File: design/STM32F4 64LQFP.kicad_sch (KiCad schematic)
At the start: 17 parts, among them P2 SWD, U1 STM32F40X_LQFP64, X2 8MHz 10ppm

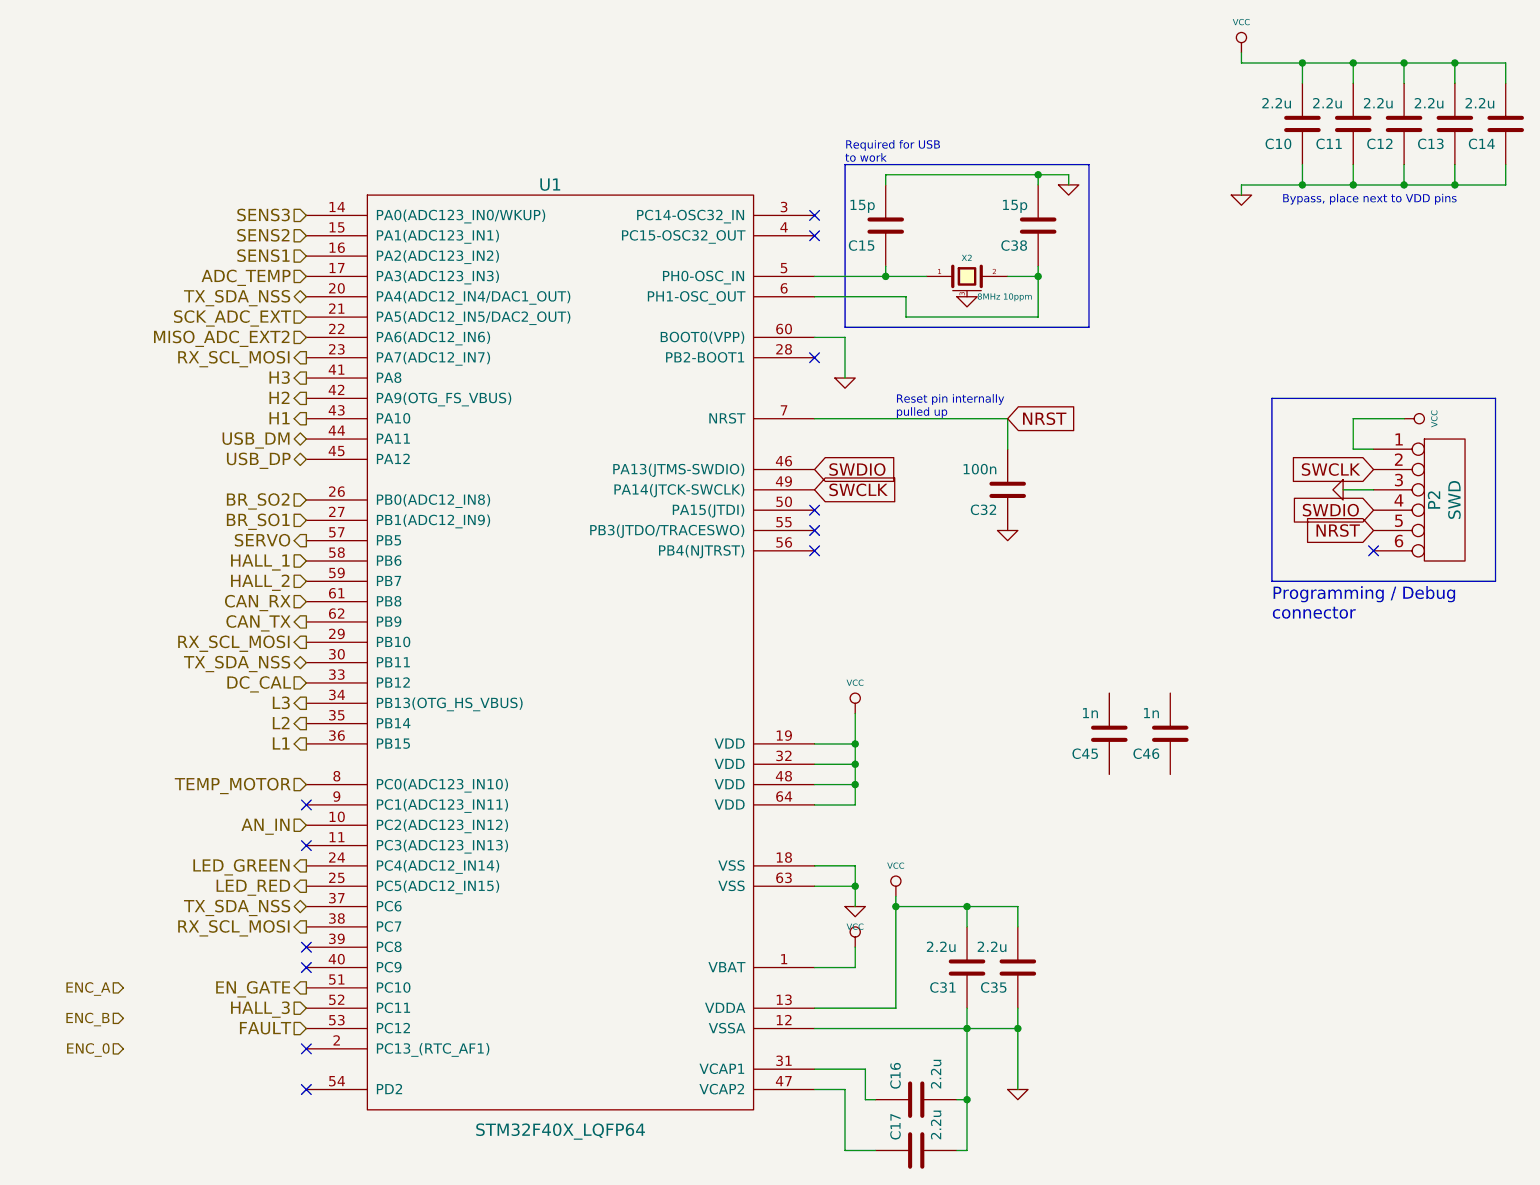
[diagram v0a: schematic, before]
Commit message: STM pins connected
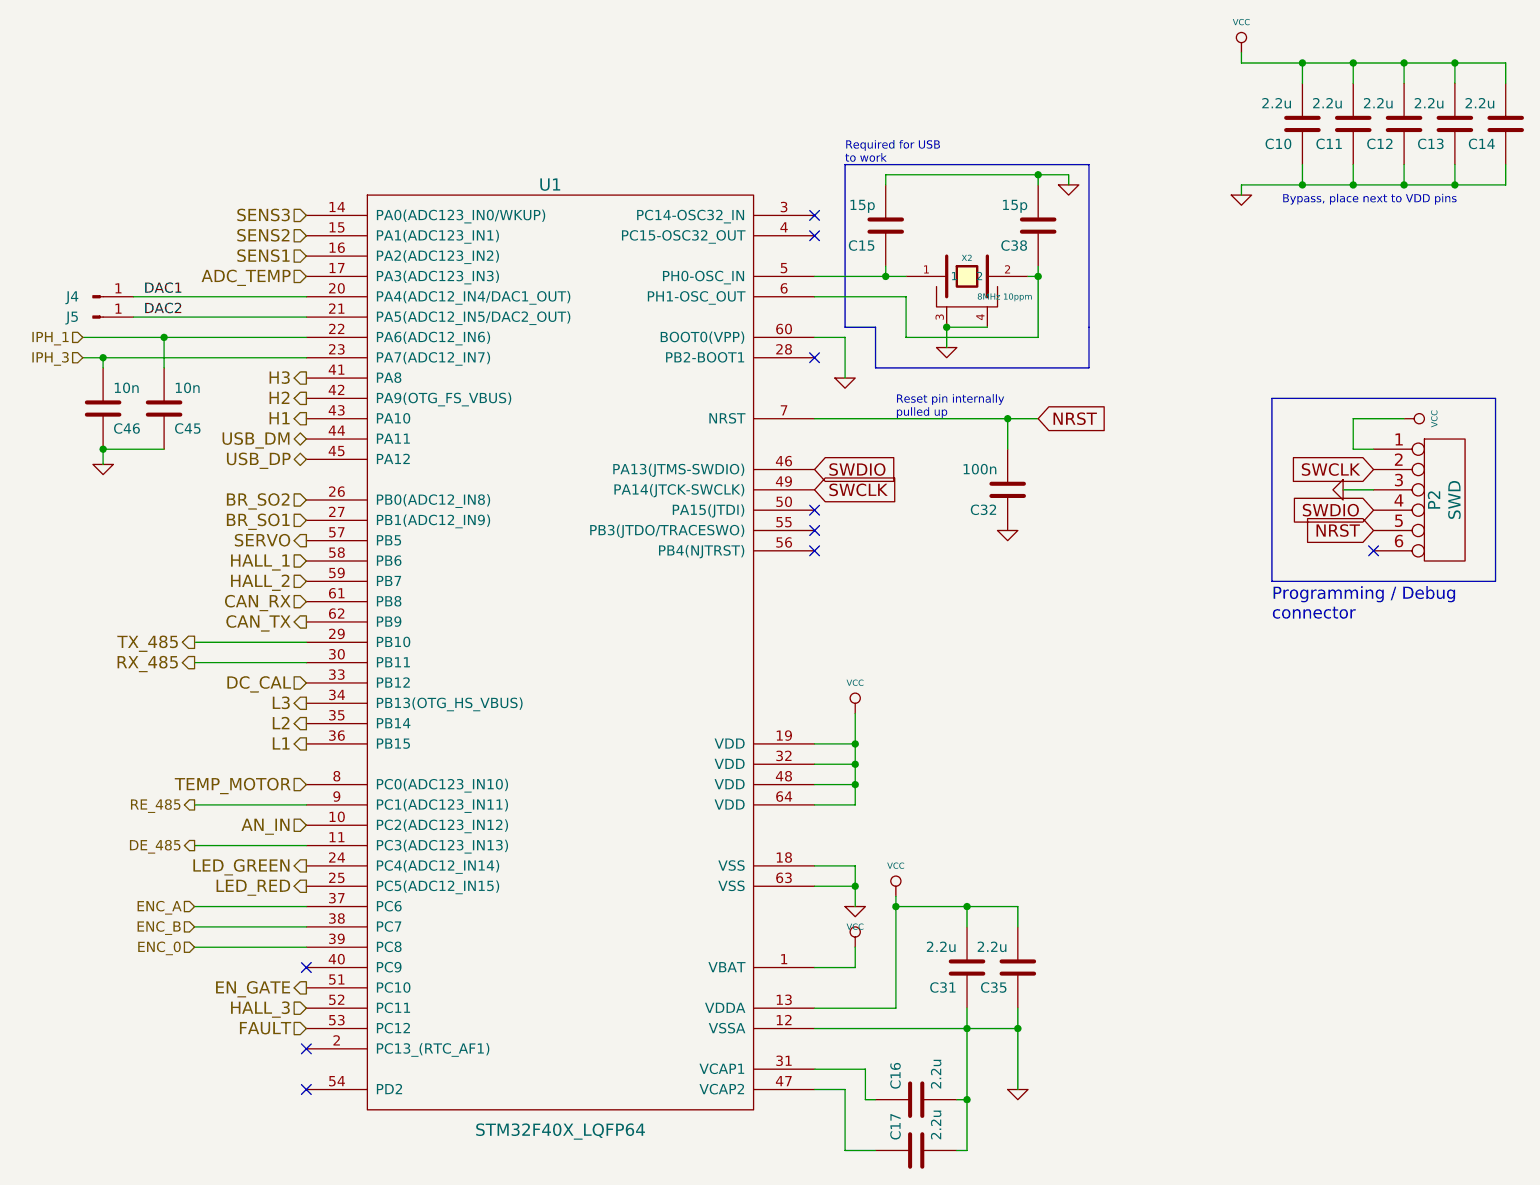
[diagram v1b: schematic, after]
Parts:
- added J4, J5: Conn_01x01_Pin, Connector_PinHeader_1.00mm:PinHeader_1x01_P1.00mm_Vertical, symbol Connector:Conn_01x01_Pin
- C45, C46: value 1n -> 10n
- X2: symbol BLDC_4-rescue:CRYSTAL_SMD -> CRF:CRYSTAL_GND24
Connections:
- net MISO_ADC_EXT2 is gone; now on net IPH_1: U1.22 (PA6(ADC12_IN6))
- net ENC_0: now also U1.39 (PC8)
- net ENC_A: now also U1.37 (PC6)
- net ENC_B: now also U1.38 (PC7)
- net GND: now also C45.1, C46.1, X2.4
- net DE_485: now reaches U1.11 (PC3(ADC123_IN13))
- net RE_485: now reaches U1.9 (PC1(ADC123_IN11))
- net IPH_3: now reaches C46.2
- net IPH_3: now also U1.23 (PA7(ADC12_IN7))
- net IPH_1: now reaches C45.2
- removed net RX_SCL_MOSI: U1.23 (PA7(ADC12_IN7)), U1.29 (PB10), U1.38 (PC7)
- net SCK_ADC_EXT renamed DAC2
- net DAC2: now also J5.1 (Pin_1)
- removed net TX_SDA_NSS: U1.20 (PA4(ADC12_IN4/DAC1_OUT)), U1.30 (PB11), U1.37 (PC6)
- new net DAC1: J4.1 (Pin_1), U1.20 (PA4(ADC12_IN4/DAC1_OUT))
- new net RX_485: U1.30 (PB11)
- new net TX_485: U1.29 (PB10)
- no-connect marks 13 -> 10
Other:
- moved on the sheet: C45, C46

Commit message: Última versão de hoje
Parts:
- P2: footprint CRF1:MICRO_JST_6 -> Connector_JST:JST_PH_B6B-PH-K_1x06_P2.00mm_Vertical
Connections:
- net DE_485: now also U1.9 (PC1(ADC123_IN11)); no longer U1.11 (PC3(ADC123_IN13))
- net RE_485: now also U1.11 (PC3(ADC123_IN13)); no longer U1.9 (PC1(ADC123_IN11))
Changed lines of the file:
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@@
     (effects (font (size 1.524 1.524)) (justify right))
   )
-  (hierarchical_label "RE_485" (shape output) (at 100.33 118.11 180) (fields_autoplaced)
+  (hierarchical_label "RE_485" (shape output) (at 100.33 123.19 180) (fields_autoplaced)
     (effects (font (size 1.27 1.27)) (justify right))
   )
@@
     (effects (font (size 1.524 1.524)) (justify right))
   )
-  (hierarchical_label "DE_485" (shape output) (at 100.33 123.19 180) (fields_autoplaced)
+  (hierarchical_label "DE_485" (shape output) (at 100.33 118.11 180) (fields_autoplaced)
     (effects (font (size 1.27 1.27)) (justify right))
   )
@@
       (effects (font (size 1.524 1.524)))
     )
-    (property "Footprint" "CRF1:MICRO_JST_6" (at 256.54 80.01 0)
-      (effects (font (size 1.524 1.524)) hide)
-    )
+    (property "Footprint" "Connector_JST:JST_PH_B6B-PH-K_1x06_P2.00mm_Vertical" (at 256.54 80.01 0)
+      (effects (font (size 1.524 1.524)) hide)
+    )

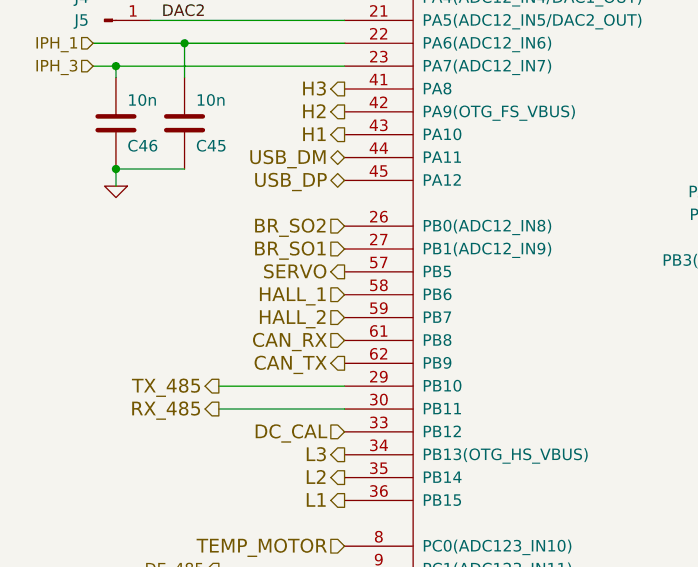
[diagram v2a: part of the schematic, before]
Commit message: Swapped SERVO and SENS1 pins
Signed-off-by: Leonardo Celente <leocelente@gmail.com>
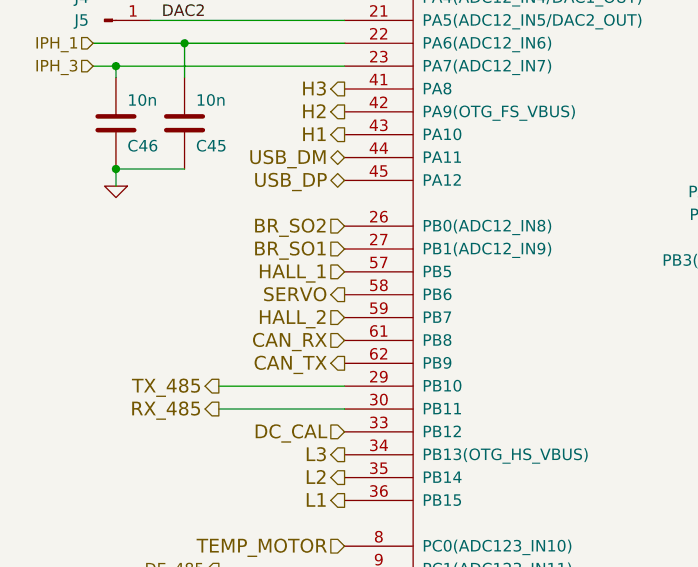
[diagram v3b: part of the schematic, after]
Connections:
- net HALL_1: now also U1.57 (PB5); no longer U1.58 (PB6)
- net SERVO: now also U1.58 (PB6); no longer U1.57 (PB5)
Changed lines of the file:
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@@
     (effects (font (size 1.524 1.524)) (justify right))
   )
-  (hierarchical_label "HALL_1" (shape input) (at 114.3 87.63 180) (fields_autoplaced)
+  (hierarchical_label "HALL_1" (shape input) (at 114.3 85.09 180) (fields_autoplaced)
     (effects (font (size 1.524 1.524)) (justify right))
   )
@@
     (effects (font (size 1.27 1.27)) (justify right))
   )
-  (hierarchical_label "SERVO" (shape output) (at 114.3 85.09 180) (fields_autoplaced)
+  (hierarchical_label "SERVO" (shape output) (at 114.3 87.63 180) (fields_autoplaced)
     (effects (font (size 1.524 1.524)) (justify right))
   )
